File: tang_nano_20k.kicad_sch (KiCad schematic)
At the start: 13 parts, among them J3 Conn_Coaxial, J4 Conn_Coaxial, J5 Conn_01x02_Pin, J6 Conn_01x02_Pin, J7 Conn_01x04_Pin, U2 Tang_Nano_20K, U5 Adafruit_PCM510x, U7 LM66100DCK

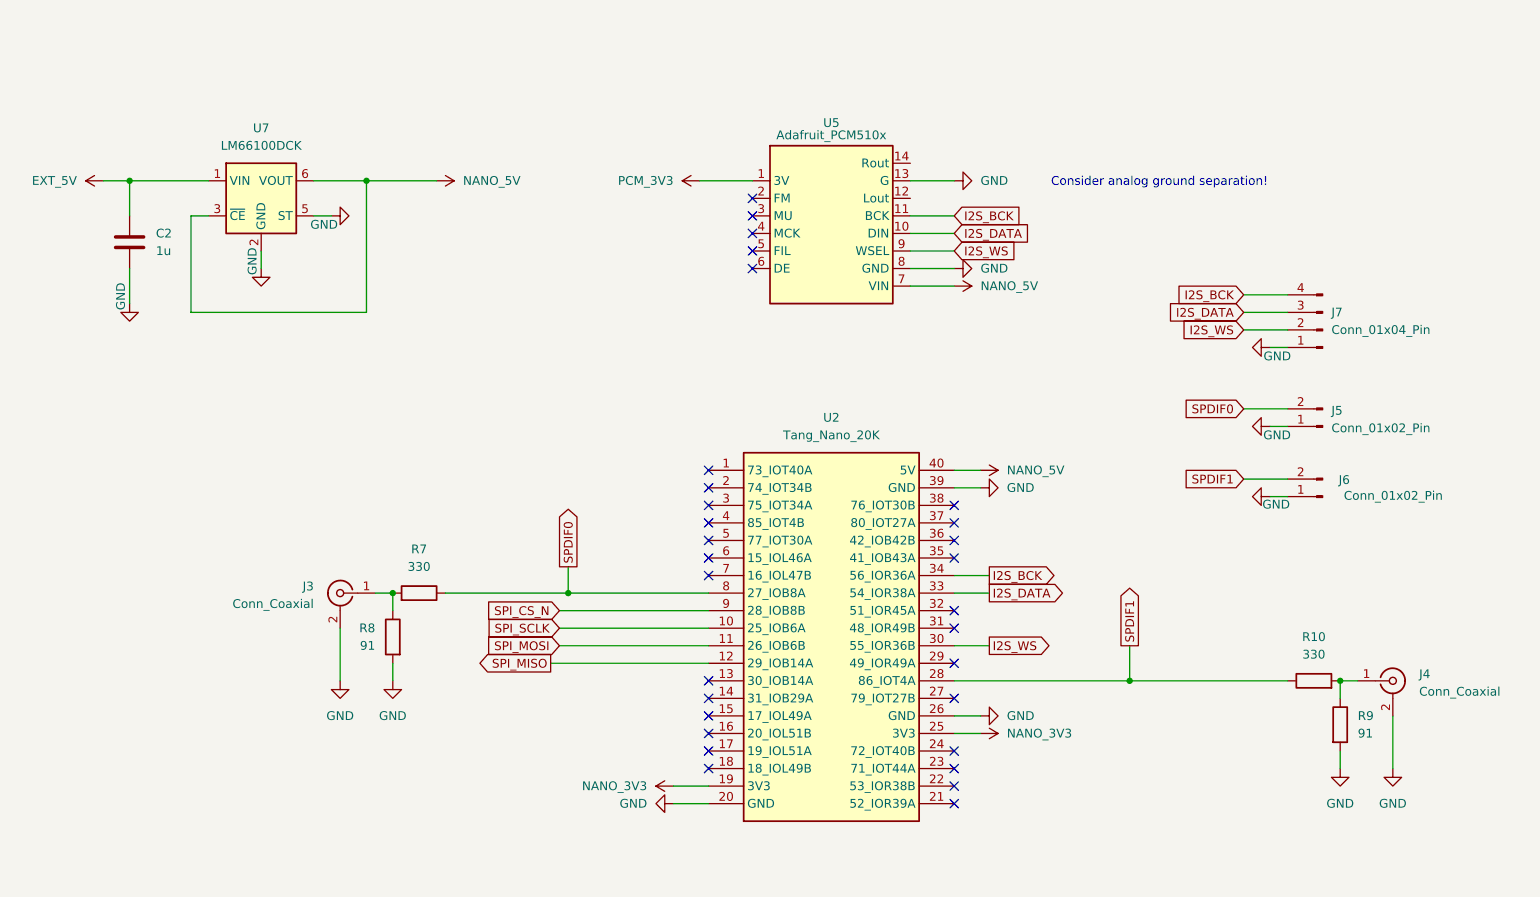
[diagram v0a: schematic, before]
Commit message: Added pin headers for SPI3, I2C0 and I2C1
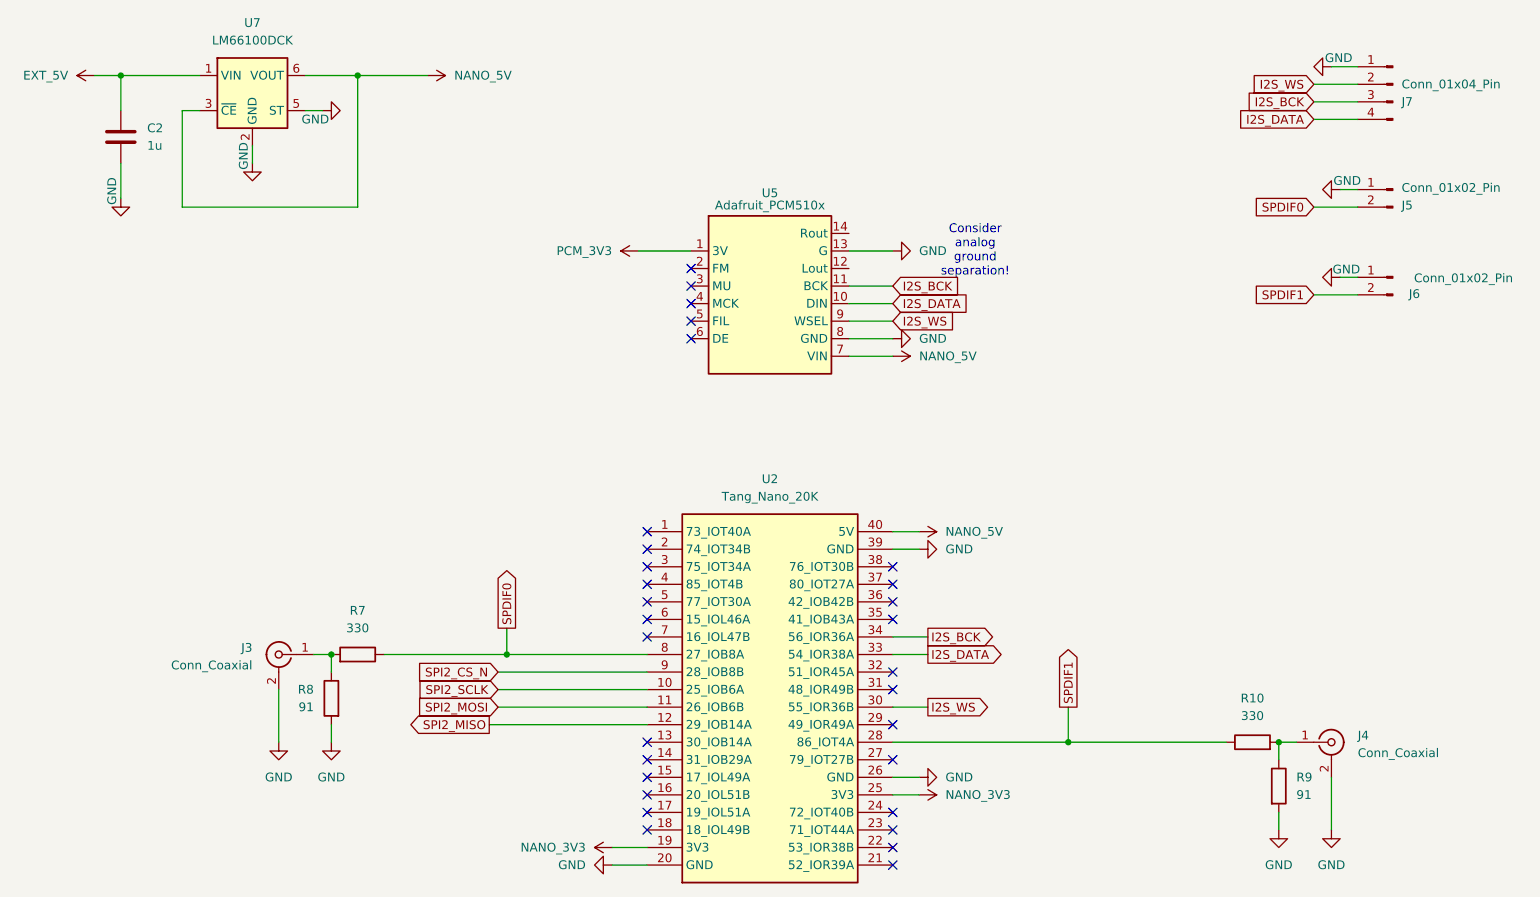
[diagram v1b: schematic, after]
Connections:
- net I2S_BCK: now also J7.3 (Pin_3); no longer J7.4 (Pin_4)
- net I2S_DATA: now also J7.4 (Pin_4); no longer J7.3 (Pin_3)
- net SPI_CS_N renamed SPI2_CS_N
- net SPI_MISO renamed SPI2_MISO
- net SPI_MOSI renamed SPI2_MOSI
- net SPI_SCLK renamed SPI2_SCLK
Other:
- moved on the sheet: C2, J3, J4, J5, J6, J7, R10, R7, R8, R9, U2, U5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

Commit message: Correcting ERC errors
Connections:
- no-connect marks 30 -> 32
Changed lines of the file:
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@@
+	)
+	(no_connect
+		(at 154.94 66.04)
 	)
 	(no_connect
@@
 	)
 	(no_connect
+		(at 154.94 71.12)
+	)
+	(no_connect

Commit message: Added jumpers for FM and FIL to DAC. Added pin headers for audio out to DAC. Minor adjustments.
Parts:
- added J13: Conn_01x03_Pin, Connector_PinHeader_2.54mm:PinHeader_1x03_P2.54mm_Vertical, symbol Connector:Conn_01x03_Pin
- added JP1, JP2: Jumper_2_Open, symbol Jumper:Jumper_2_Open
- C2: footprint (none) -> Capacitor_THT:C_Disc_D5.0mm_W2.5mm_P5.00mm
- R10, R7, R8, R9: footprint (none) -> Resistor_THT:R_Axial_DIN0207_L6.3mm_D2.5mm_P10.16mm_Horizontal
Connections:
- net GND: no longer U5.13 (G)
- net PCM_3V3: now also JP1.1 (A), JP2.1 (A)
- net at U5.12 (Lout): now also J13.2 (Pin_2)
- net at U5.14 (Rout): now also J13.3 (Pin_3)
- net at U5.2 (FM): now also JP2.2 (B)
- net at U5.5 (FIL): now also JP1.2 (B)
- new net: J13.1 (Pin_1), U5.13 (G)
- no-connect marks 32 -> 28
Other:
- note removed: "Consider analog ground separation!"

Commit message: Added footprints for DAC jumpers.
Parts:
- JP1, JP2: footprint (none) -> Connector_PinHeader_2.54mm:PinHeader_1x02_P2.54mm_Vertical
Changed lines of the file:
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@@
 			)
 		)
-		(property "Footprint" ""
+		(property "Footprint" "Connector_PinHeader_2.54mm:PinHeader_1x02_P2.54mm_Vertical"
 			(at 121.92 71.12 0)
 			(hide yes)
@@
 			)
 		)
-		(property "Footprint" ""
+		(property "Footprint" "Connector_PinHeader_2.54mm:PinHeader_1x02_P2.54mm_Vertical"
 			(at 121.92 78.74 0)
 			(hide yes)

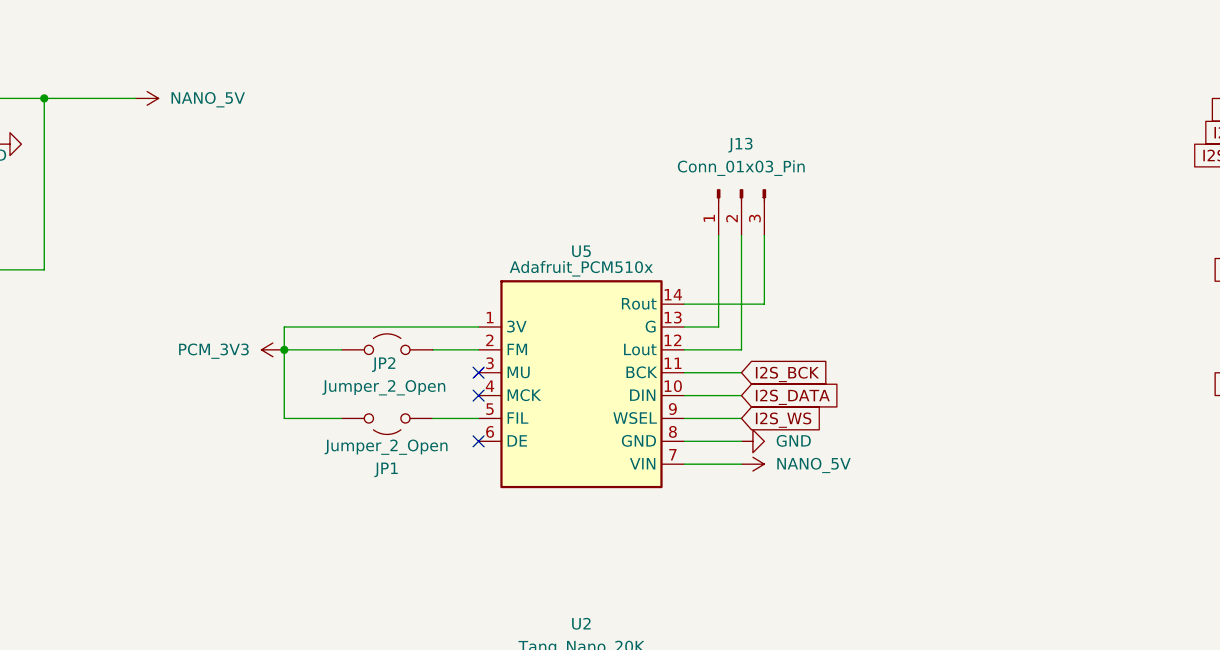
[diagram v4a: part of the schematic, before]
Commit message: All parts now have footprints.
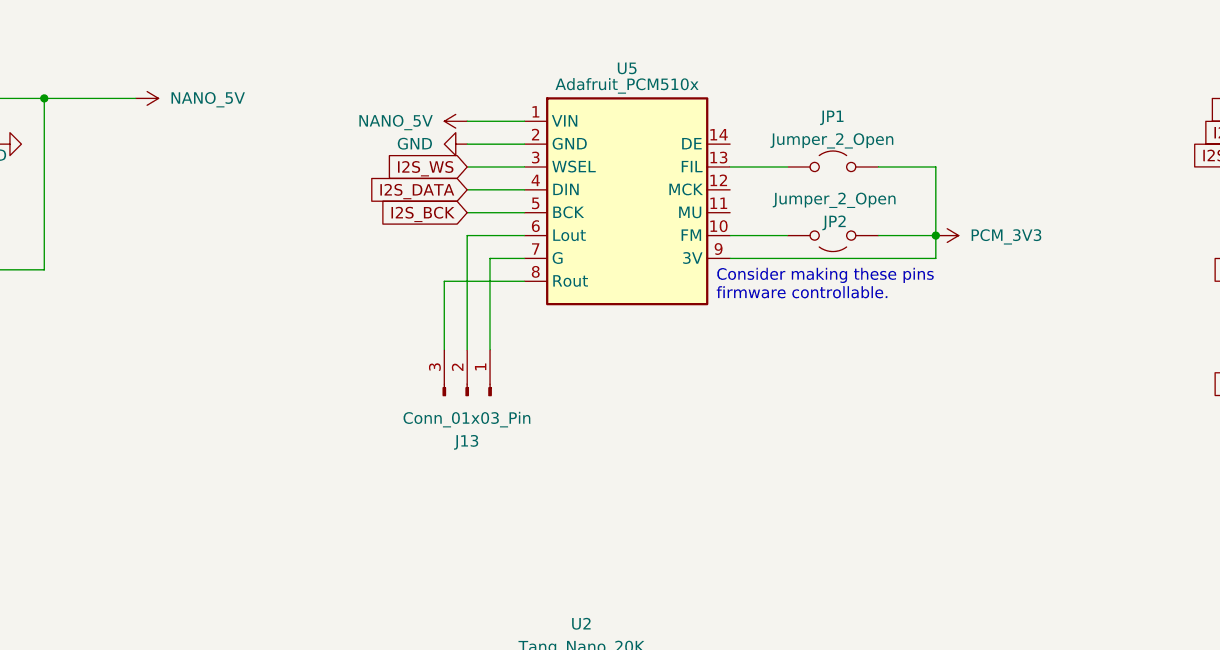
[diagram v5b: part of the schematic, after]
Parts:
- J6: footprint Connector_PinHeader_2.54mm:PinHeader_1x02_P2.54mm_Vertical_SMD_Pin1Left -> Connector_PinHeader_2.54mm:PinHeader_1x02_P2.54mm_Vertical
- U5: footprint (none) -> noaidi-fpga-synth:Adafruit_PCM510x
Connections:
- net GND: now also U5.2 (GND); no longer U5.8 (GND)
- net I2S_BCK: now also U5.5 (BCK); no longer U5.11 (BCK)
- net I2S_DATA: now also U5.4 (DIN); no longer U5.10 (DIN)
- net I2S_WS: now also U5.3 (WSEL); no longer U5.9 (WSEL)
- net NANO_5V: now also U5.1 (VIN); no longer U5.7 (VIN)
- net PCM_3V3: now also U5.9 (3V); no longer U5.1 (3V)
- net at JP2.2 (B): now also U5.10 (FM); no longer U5.2 (FM)
- net at U5.12 (MCK): no longer J13.2 (Pin_2)
- net at U5.13 (FIL): now also JP1.2 (B); no longer J13.1 (Pin_1)
- net at U5.14 (DE): no longer J13.3 (Pin_3)
- net at U5.6 (Lout): now also J13.2 (Pin_2)
- new net: J13.1 (Pin_1), U5.7 (G)
- new net: J13.3 (Pin_3), U5.8 (Rout)
- no-connect marks 28 -> 25
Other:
- note added: "Consider making these pins firmware controllable."
- moved on the sheet: J13, JP1, JP2, U5

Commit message: Completely routed PCB
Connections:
- net NANO_3V3: no longer U2.19 (3V3)
- no-connect marks 25 -> 26
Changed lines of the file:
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@@
+	)
+	(no_connect
+		(at 125.73 154.94)
 	)
 	(no_connect
@@
 		(pts
 			(xy 104.14 134.62) (xy 125.73 134.62)
-		)
-		(stroke
-			(width 0)
-			(type default)
-		)
-	)
-	(wire
-		(pts
-			(xy 120.65 154.94) (xy 125.73 154.94)
 		)
 		(stroke
@@
 					(unit 1)
 				)
-			)
-		)
-	)
-	(symbol
-		(lib_id "power:+5V")
-		(at 120.65 154.94 90)
-		(mirror x)
-		(unit 1)
-		(body_style 1)
-		(exclude_from_sim no)
-		(in_bom yes)
-		(on_board yes)
-		(in_pos_files yes)
-		(dnp no)
-		(property "Reference" "#PWR016"
-			(at 124.46 154.94 0)
-			(hide yes)
-			(show_name no)
-			(do_not_autoplace no)
-			(effects
-				(font
-					(size 1.27 1.27)
-				)
-			)
-		)
-		(property "Value" "NANO_3V3"
-			(at 116.84 154.9399 90)
-			(show_name no)
-			(do_not_autoplace no)
-			(effects
-				(font
-					(size 1.27 1.27)
-				)
-				(justify left)
-			)
-		)
-		(property "Footprint" ""
-			(at 120.65 154.94 0)
-			(hide yes)
-			(show_name no)
-			(do_not_autoplace no)
-			(effects
-				(font
-					(size 1.27 1.27)
-				)
-			)
-		)
-		(property "Datasheet" ""
-			(at 120.65 154.94 0)
-			(hide yes)
-			(show_name no)
-			(do_not_autoplace no)
-			(effects
-				(font
-					(size 1.27 1.27)
-				)
-			)
-		)
-		(property "Description" "Power symbol creates a global label with name \"+5V\""
-			(at 120.65 154.94 0)
-			(hide yes)
-			(show_name no)
-			(do_not_autoplace no)
-			(effects
-				(font
-					(size 1.27 1.27)
-				)
-			)
-		)
-		(pin "1"
-		)
-		(instances
-			(project "noaidi-fpga-synth"
-				(path "/549f0467-9724-4494-baa6-490c1a442987"
-					(reference "#PWR016")
-					(unit 1)
-				)
